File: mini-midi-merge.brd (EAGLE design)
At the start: 139.7 x 20.2 mm, 66 parts, among them IC1 REG1117, X5 DIN5PIN

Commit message: almost done
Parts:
- removed U$1: PIC16F1825SO14, jasons_stuff:SO14
- added IC5: REG1117, burr-brown:SOT223
- IC1: value REG1117 -> PIC16F1825SO14; device burr-brown:SOT223 -> jasons_stuff:SO14
- moved R26 107.1 mm to (6.35, 3.81), turned to 90 degrees
- moved R22 101.1 mm to (24.1, 16.4), turned to 270 degrees
- moved C1 94.2 mm to (114.6, 8.64), turned to 0 degrees
- moved R7 90.2 mm to (96.5, 3.81), turned to 270 degrees
- moved R21 89.5 mm to (30.5, 3.81), turned to 90 degrees
- moved R4 89.5 mm to (118.9, 17.9), turned to 0 degrees
- moved R17 80.6 mm to (46.9, 16.5), turned to 270 degrees
- moved R5 79.4 mm to (112.5, 17.9), turned to 0 degrees
- moved R1 76.6 mm to (129.9, 4.70), turned to 270 degrees
- moved R16 76.6 mm to (53.3, 3.81), turned to 90 degrees
- moved R8 75.7 mm to (86.2, 14.0), turned to 180 degrees
- moved R3 71.9 mm to (125.2, 17.9), turned to 180 degrees
- moved C5 71.4 mm to (43.6, 16.5), turned to 270 degrees
- moved R2 70.6 mm to (126.6, 4.70), turned to 90 degrees
- moved R6 69.5 mm to (99.1, 3.81), turned to 270 degrees
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- renumbered G1 to IC11, J1 to ICSP4, J2 to ICSP3, J3 to ICSP2, J4 to ICSP1, LED1 to L1, LED2 to L2, LED3 to L3, LED4 to L4, LED5 to L6, LED6 to L7, LED7 to L5, OK1 to IC9, OK2 to IC8, OK3 to IC7, OK4 to IC10, U$2 to IC4, U$3 to IC3, U$4 to IC2, U$5 to D2, U$6 to D3, U$7 to D4, U$8 to D1
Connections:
- net GND: now also C1.1, C6.2, IC1.14, IC5.1, R13.2, R15.2, R17.1, R18.2, R20.2, R22.1; no longer C1.2, C6.1, IC1.1, R13.1, R14.1, R2.2, R24.2, R5.2, R8.2, U$1.14
- net MIDI_IN0: now also IC1.5, R9.1; no longer R12.1, U$1.5
- net MIDI_IN1: now also R24.1; no longer R9.1
- net MIDI_IN2: now also R19.1; no longer R6.1
- net MIDI_IN3: now also R14.1; no longer R3.1
- net MIDI_OUT: now also IC1.6, R1.1; no longer R16.1, U$1.6
- net N$1: now also R16.1; no longer R1.1
- net N$10: now also R26.2; no longer R7.2
- net N$12: now also R25.1; no longer R8.1
- net N$13: now also R12.1; no longer R10.1
- net N$14: now also R12.2; no longer R10.2
- net N$17: now also R17.2; no longer R14.2
- net N$18: now also R22.2; no longer R13.2
- net N$19: now also R8.1; no longer R20.1
- net N$2: now also R16.2; no longer R1.2
- net N$20: now also C1.2, C8.+, IC5.3; no longer C5.2, C7.+, IC1.3
- net N$21: now also R3.1; no longer R22.1
- net N$22: now also R1.2; no longer R16.2
- net N$26: now also R18.1; no longer R24.1
- net N$27: now also R10.2; no longer R15.2
- net N$28: now also R2.1; no longer R17.1
- net N$31: now also R13.1; no longer R25.1
- net N$32: now also IC1.4; no longer U$1.4
- net N$33: now also R4.1; no longer R21.1
- net N$34: now also IC1.13; no longer U$1.13
- net N$35: now also IC1.12; no longer U$1.12
- net N$36: now also IC1.8, R8.2; no longer R20.2, U$1.8
- net N$37: now also IC1.11, R4.2; no longer R21.2, U$1.11
- net N$4: now also R21.1; no longer R4.1
- net N$40: now also IC1.2; no longer U$1.2
- net N$41: now also IC1.7, R5.2; no longer R26.2, U$1.7
- net N$42: now also R5.1; no longer R26.1
- net N$5: now also R15.1; no longer R2.1
- net N$6: now also R21.2; no longer R4.2
- net N$8: now also R20.1; no longer R5.1
- net N$9: now also R26.1; no longer R7.1
- net SCL: now also IC1.10, R6.1; no longer R18.1, U$1.10
- net SDA: now also IC1.9, R7.1; no longer R19.1, U$1.9
- net VCC: now also C5.2, C6.1, C7.+, IC1.1, IC5.2, R10.1, R14.2, R2.2, R24.2, R7.2; no longer C1.1, C6.2, C8.+, IC1.2, R12.2, R15.1, R17.2, R18.2, R22.2, U$1.1
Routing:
- net N$32: track 19.1 -> 11.7 mm, vias 1 -> 2
- net N$34: track 7.05 -> 12.4 mm, vias 1 -> 2
- net N$35: track 6.42 -> 3.11 mm, vias 1 -> 0
- net N$25: track 13.7 -> 16.2 mm
- net N$31: track 2.10 -> 4.30 mm
- net MIDI_IN3: track 20.0 -> 17.9 mm
- net N$37: track 35.2 -> 33.4 mm
- net SCL: track 120.2 -> 118.6 mm
- net GND: track 60.1 -> 59.1 mm
- net VCC: track 250.7 -> 251.5 mm, vias 5 -> 6
- net N$19: track 4.42 -> 5.16 mm
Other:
- board text added: "4:1 midi merge"
- board text added: "hotchk155"
- board text added: "rev 1"

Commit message: ground output pin 2
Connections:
- net GND: now also X5.2
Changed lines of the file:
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@@
 <layer number="20" name="Dimension" color="15" fill="1" visible="yes" active="yes"/>
 <layer number="21" name="tPlace" color="7" fill="1" visible="yes" active="yes"/>
-<layer number="22" name="bPlace" color="7" fill="1" visible="no" active="yes"/>
+<layer number="22" name="bPlace" color="7" fill="1" visible="yes" active="yes"/>
 <layer number="23" name="tOrigins" color="15" fill="1" visible="yes" active="yes"/>
-<layer number="24" name="bOrigins" color="15" fill="1" visible="no" active="yes"/>
+<layer number="24" name="bOrigins" color="15" fill="1" visible="yes" active="yes"/>
 <layer number="25" name="tNames" color="7" fill="1" visible="yes" active="yes"/>
-<layer number="26" name="bNames" color="7" fill="1" visible="no" active="yes"/>
+<layer number="26" name="bNames" color="7" fill="1" visible="yes" active="yes"/>
 <layer number="27" name="tValues" color="7" fill="1" visible="yes" active="yes"/>
-<layer number="28" name="bValues" color="7" fill="1" visible="no" active="yes"/>
-<layer number="29" name="tStop" color="7" fill="3" visible="no" active="yes"/>
-<layer number="30" name="bStop" color="7" fill="6" visible="no" active="yes"/>
-<layer number="31" name="tCream" color="7" fill="4" visible="no" active="yes"/>
-<layer number="32" name="bCream" color="7" fill="5" visible="no" active="yes"/>
-<layer number="33" name="tFinish" color="6" fill="3" visible="no" active="yes"/>
-<layer number="34" name="bFinish" color="6" fill="6" visible="no" active="yes"/>
-<layer number="35" name="tGlue" color="7" fill="4" visible="no" active="yes"/>
-<layer number="36" name="bGlue" color="7" fill="5" visible="no" active="yes"/>
+<layer number="28" name="bValues" color="7" fill="1" visible="yes" active="yes"/>
+<layer number="29" name="tStop" color="7" fill="3" visible="yes" active="yes"/>
+<layer number="30" name="bStop" color="7" fill="6" visible="yes" active="yes"/>
+<layer number="31" name="tCream" color="7" fill="4" visible="yes" active="yes"/>
+<layer number="32" name="bCream" color="7" fill="5" visible="yes" active="yes"/>
+<layer number="33" name="tFinish" color="6" fill="3" visible="yes" active="yes"/>
+<layer number="34" name="bFinish" color="6" fill="6" visible="yes" active="yes"/>
+<layer number="35" name="tGlue" color="7" fill="4" visible="yes" active="yes"/>
+<layer number="36" name="bGlue" color="7" fill="5" visible="yes" active="yes"/>
 <layer number="37" name="tTest" color="7" fill="1" visible="yes" active="yes"/>
 <layer number="38" name="bTest" color="7" fill="1" visible="yes" active="yes"/>
-<layer number="39" name="tKeepout" color="4" fill="11" visible="no" active="yes"/>
-<layer number="40" name="bKeepout" color="1" fill="11" visible="no" active="yes"/>
-<layer number="41" name="tRestrict" color="4" fill="10" visible="no" active="yes"/>
-<layer number="42" name="bRestrict" color="1" fill="10" visible="no" active="yes"/>
-<layer number="43" name="vRestrict" color="2" fill="10" visible="no" active="yes"/>
+<layer number="39" name="tKeepout" color="4" fill="11" visible="yes" active="yes"/>
+<layer number="40" name="bKeepout" color="1" fill="11" visible="yes" active="yes"/>
+<layer number="41" name="tRestrict" color="4" fill="10" visible="yes" active="yes"/>
+<layer number="42" name="bRestrict" color="1" fill="10" visible="yes" active="yes"/>
+<layer number="43" name="vRestrict" color="2" fill="10" visible="yes" active="yes"/>
 <layer number="44" name="Drills" color="7" fill="1" visible="yes" active="yes"/>
 <layer number="45" name="Holes" color="7" fill="1" visible="yes" active="yes"/>
@@
 <layer number="50" name="dxf" color="7" fill="1" visible="no" active="no"/>
 <layer number="51" name="tDocu" color="7" fill="1" visible="yes" active="yes"/>
-<layer number="52" name="bDocu" color="7" fill="1" visible="no" active="yes"/>
+<layer number="52" name="bDocu" color="7" fill="1" visible="yes" active="yes"/>
 <layer number="53" name="tGND_GNDA" color="7" fill="9" visible="no" active="no"/>
 <layer number="54" name="bGND_GNDA" color="1" fill="9" visible="no" active="no"/>
@@
 </polygon>
 <via x="93.218" y="15.24" extent="1-16" drill="0.6"/>
+<contactref element="X5" pad="2"/>
 </signal>
 <signal name="N$4">

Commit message: adding comp values
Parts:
- R1, R12, R16, R2, R21, R26: value (none) -> 220
- R10, R17, R22: value (none) -> 10k
- R11, R14, R15, R19, R20, R24, R25, R9: value (none) -> 1k5
- R13, R18, R23, R3, R4, R5, R8: value (none) -> 1k
- R6, R7: value (none) -> 4k7

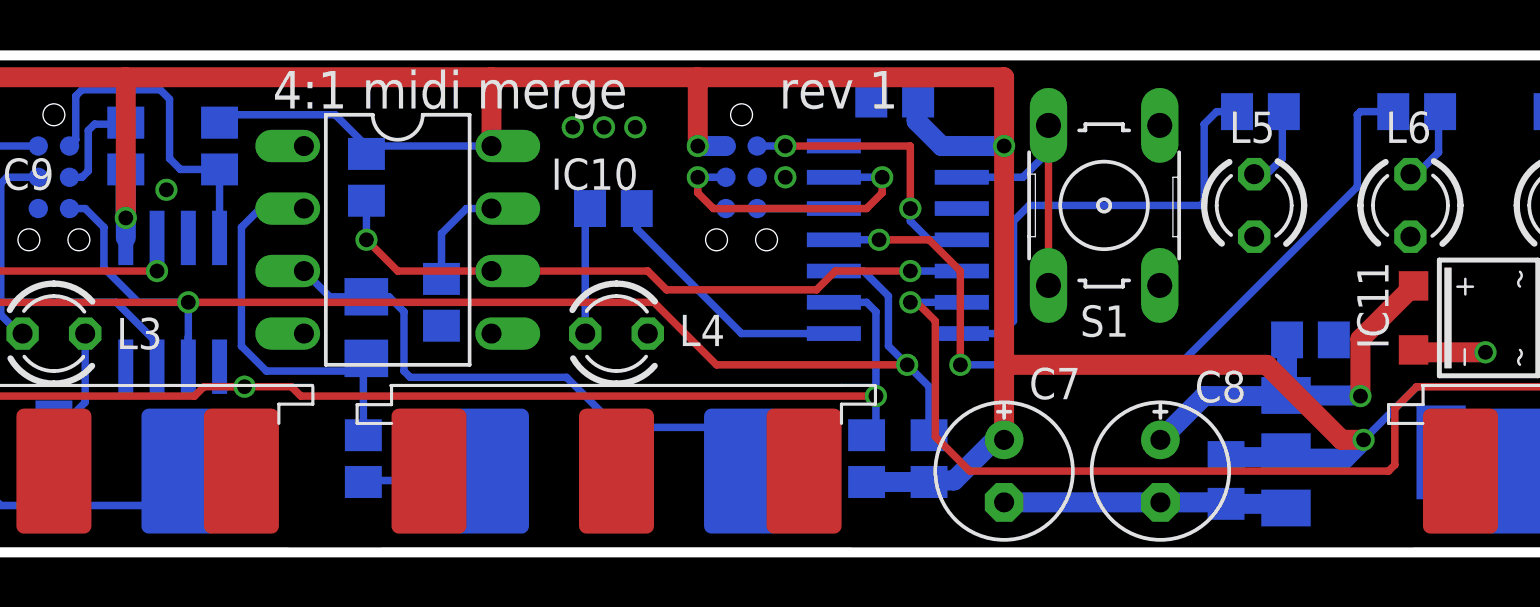
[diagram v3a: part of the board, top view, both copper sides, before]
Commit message: PCB REV2
move switch to match bsplit
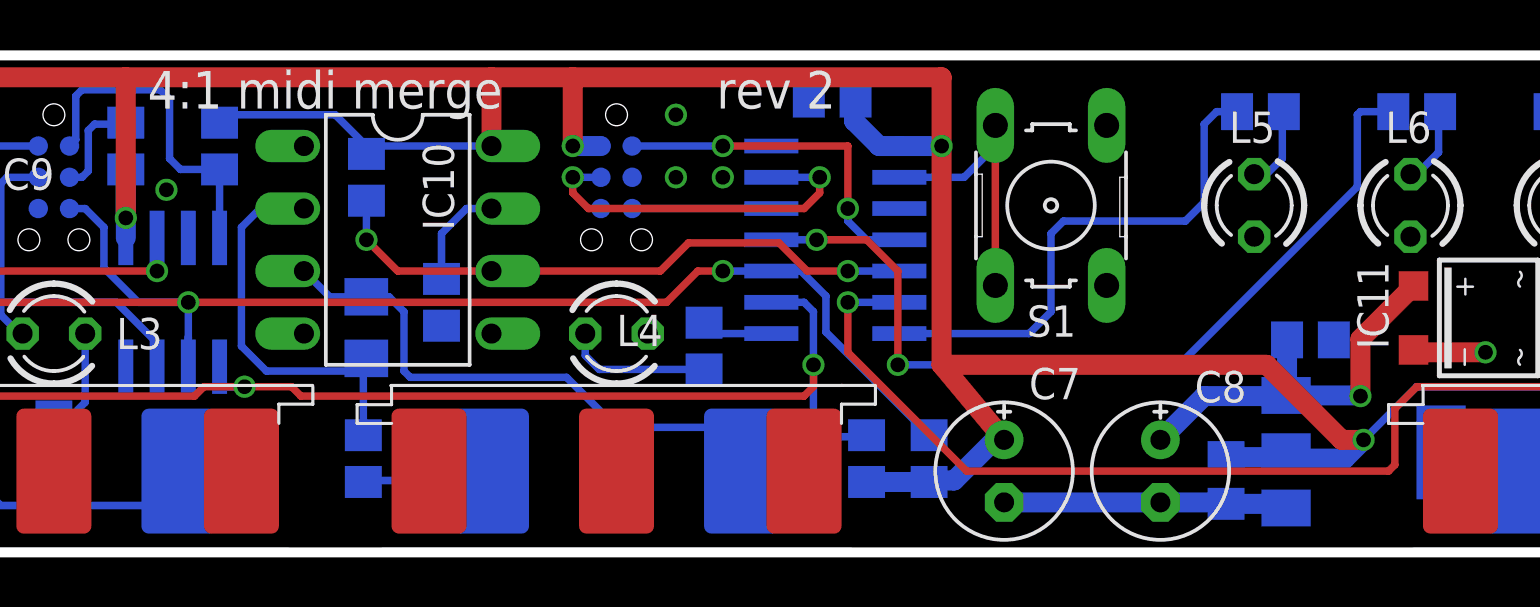
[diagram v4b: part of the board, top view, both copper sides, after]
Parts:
- moved R8 6.69 mm to (89.9, 8.38), turned to 90 degrees
- moved ICSP1 5.08 mm to (86.4, 17.8)
- moved IC1 2.54 mm to (95.2, 12.7)
- moved C3 2.54 mm to (95.1, 18.4)
- moved S1 2.16 mm to (104.0, 14.1)
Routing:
- net N$36: track 10.6 -> 2.92 mm
- net SCL: track 118.6 -> 113.6 mm
- net N$35: track 3.11 -> 5.66 mm
- net N$34: track 12.4 -> 14.9 mm
- net N$37: track 33.4 -> 35.9 mm
- net N$32: track 11.7 -> 14.2 mm
- net MIDI_IN0: track 26.9 -> 24.7 mm
- net N$41: track 19.2 -> 21.2 mm
- net MIDI_OUT: track 43.7 -> 44.7 mm
- net VCC: track 251.5 -> 252.5 mm
- net SDA: track 85.0 -> 85.9 mm
- net N$19: track 5.16 -> 5.95 mm
- net GND: vias 13 -> 12
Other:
- board text added: "rev 2"
- board text removed: "rev 1"
